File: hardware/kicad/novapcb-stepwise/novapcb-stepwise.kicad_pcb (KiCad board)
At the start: 6 copper layers, 105 x 85 mm, 129 parts, among them J1 USB-C_2.0, J10 CRSF_solder_pad, J11 ESC_solder_pad, J12 ESC_solder_pad, J13 ESC_solder_pad, J14 ESC_solder_pad, J15 ESC_solder_pad, J16 ESC_solder_pad, J17 ESC_solder_pad, J18 ESC_solder_pad, J19 MAUCH2_6P, J2 microSD_DM3AT, J20 CAN_4P, J3 TELEM_6P, J4 MAUCH_6P, J5 GPS_MAG_10P, J9 SWD_10P, Q2 AO3401A, Q3 AO4262E, Q4 AO4262E, Q5 AO3400A, U1 STM32H743VITx, U11 LM74700-Q1, U12 LM74700-Q1, U13 LP5907MFX-3.3, U14 TJA1051TK/3, U15 PESD2CAN, U2 AP2112K-3.3, U3 ICM-42688-P_LGA-14_2.5x3mm_P0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, U4 DPS310, U5 USBLC6-2P6, U6 TPS25940A, U7 LPS22HB, U8 BMI088, U9 LSM6DSV16X, Y1 8MHz

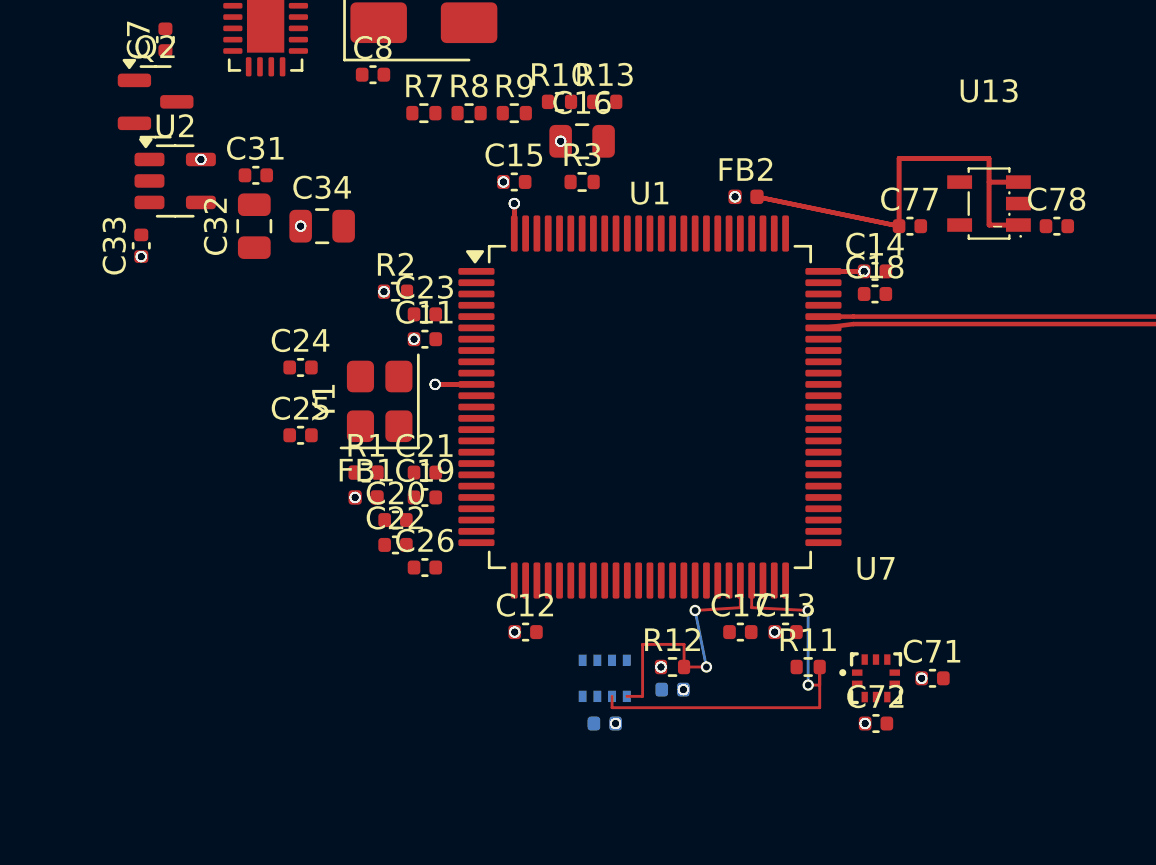
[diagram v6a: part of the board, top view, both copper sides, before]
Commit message: docs+hw: v1.1 6-layer stackup locked, +3V3 moved In4→In3 for B.Cu GND ref
Per master 2026-05-23 directive: articulated per-layer assignment with
explicit SI rationale BEFORE A↔B routing commits a second power plane.

## Final v1.1 stackup (DECISIONS §8)

  L1 F.Cu      — components + high-speed signals (USB diff, I2C2, SPI, DShot)
  L2 In1.Cu    — GND plane (primary)
  L3 In2.Cu    — +5V_BEC plane (NEW for A↔B routing)
  L4 In3.Cu    — +3V3 plane (MOVED from In4 — for B.Cu reference SI)
  L5 In4.Cu    — GND plane (secondary)
  L6 B.Cu      — signals (B.Cu USB sliver, I2C2 sliver, future SDMMC1)

Two GND planes (L2 + L5) sandwich the two power planes. Each signal
layer (L1, L6) has its adjacent reference plane = GND. The two power
planes (L3 +5V, L4 +3V3) are inner-adjacent — they share inter-plane
capacitance as a free HF decoupling cap between rails (acceptable
since +3V3 is derived from +5V via U2 LDO, not DC-isolated).

## Why move +3V3 from In4 to In3

Original PR #72 placed +3V3 on In4. With +3V3 on In4 and B.Cu signals
on L6, B.Cu signals reference +3V3 (not GND). For B.Cu's current 1-2mm
USB diff slivers this is "good enough" but compromises principled SI
for future SDMMC1 (50 MHz) and other high-speed B.Cu routes.

Moving +3V3 to In3 (and putting GND on In4) gives B.Cu a clean GND
reference. Trivial implementation cost: change SetLayer(IN4_CU) to
SetLayer(IN3_CU) in integ_C_B.py.

Thermal impact: zero (gate12 power-injection is layer-independent;
energy balance unaffected).

## SI verification per layer

  F.Cu (L1) → L2 In1 GND adjacent, 0.21mm prepreg — optimal for USB
    87Ω diff pair, I2C2, SPI, DShot.
  B.Cu (L6) → L5 In4 GND adjacent, 0.21mm prepreg — optimal for
    USB B.Cu slivers and future SDMMC1.

Power planes well-decoupled:
  L3 +5V_BEC → L2 GND adjacent above
  L4 +3V3    → L5 GND adjacent below

## Alternatives rejected

| Alternative | Issue |
|---|---|
| 1 GND + 2 power | B.Cu signals see power plane → SI compromise |
| GND-pwr-GND-pwr-GND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
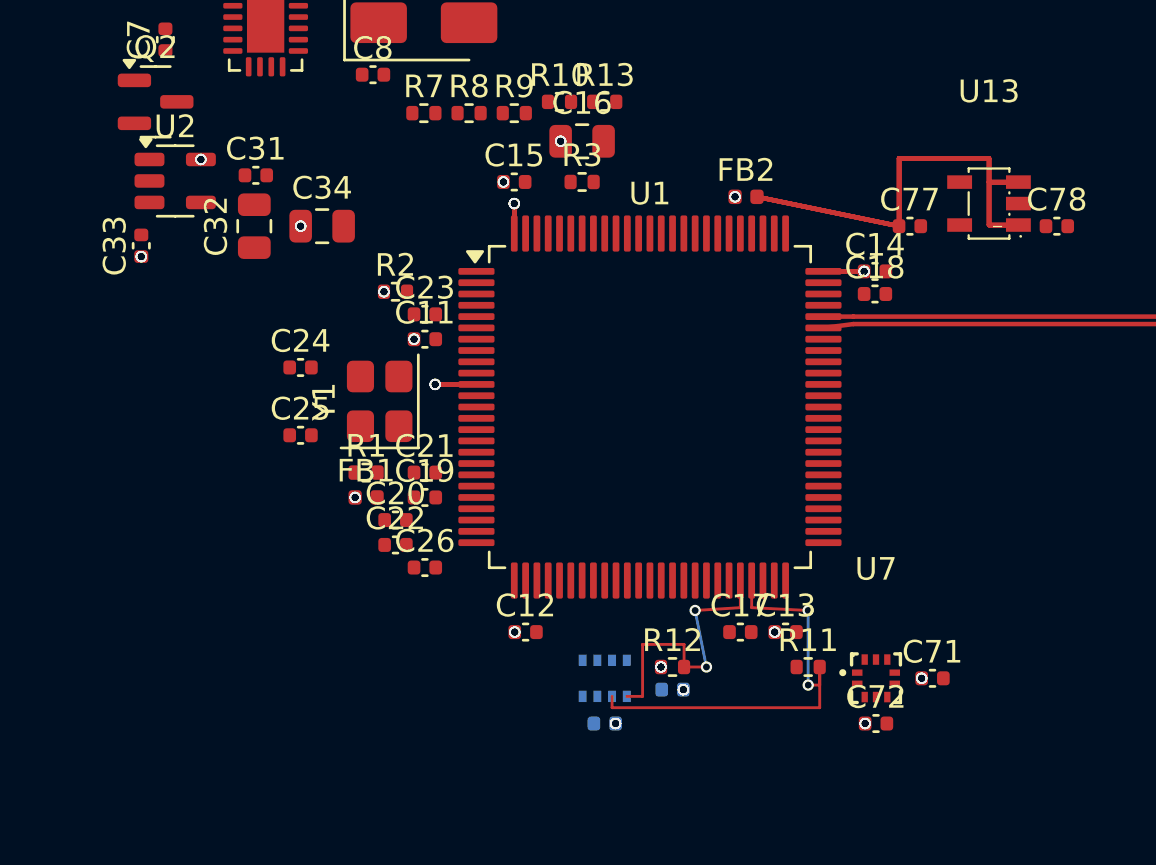
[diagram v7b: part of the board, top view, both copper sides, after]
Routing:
- net +3V3_IMU_PRE: track 37.9 -> 56.8 mm
- net +3V3: track 9.91 -> 14.9 mm, vias 38 -> 57
- added copper zone on In3.Cu, net +3V3
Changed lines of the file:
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@@
+	)
+	(segment
+		(start 52.675 29)
+		(end 54.48 29)
+		(width 0.2)
+		(layer "F.Cu")
+		(net 1)
 	)
 	(segment
@@
 	)
 	(segment
+		(start 39 27.325)
+		(end 39 26)
+		(width 0.2)
+		(layer "F.Cu")
+		(net 1)
+	)
+	(segment
 		(start 37.325 34)
 		(end 35.5 34)
@@
 	)
 	(segment
+		(start 37.325 34)
+		(end 35.5 34)
+		(width 0.2)
+		(layer "F.Cu")
+		(net 1)
+	)
+	(segment
 		(start 52.675 29)
 		(end 54.48 29)
@@
 	)
 	(via
+		(at 29.55 27)
+		(size 0.5)
+		(drill 0.3)
+		(layers "F.Cu" "B.Cu")
+		(net 1)
+	)
+	(via
 		(at 22.5 28.346025)
 		(size 0.5)
@@
 	)
 	(via
+		(at 45.49 46.5)
+		(size 0.5)
+		(drill 0.3)
+		(layers "F.Cu" "B.Cu")
+		(net 1)
+	)
+	(via
 		(at 41.05 23.245)
 		(size 0.5)
@@
 	)
 	(via
+		(at 34.564999 32)
+		(size 0.5)
+		(drill 0.3)
+		(layers "F.Cu" "B.Cu")
+		(net 1)
+	)
+	(via
 		(at 45.49 46.5)
 		(size 0.5)
@@
 	)
 	(via
+		(at 54.475 29)
+		(size 0.5)
+		(drill 0.3)
+		(layers "F.Cu" "B.Cu")
+		(net 1)
+	)
+	(via
 		(at 29.55 27)
 		(size 0.5)
@@
 	)
 	(via
+		(at 39.02 44.955)
+		(size 0.5)
+		(drill 0.3)
+		(layers "F.Cu" "B.Cu")
+		(net 1)
+	)
+	(via
 		(at 38.52 25.045)
 		(size 0.5)
@@
 	)
 	(via
+		(at 39 26)
+		(size 0.5)
+		(drill 0.3)
+		(layers "F.Cu" "B.Cu")
+		(net 1)
+	)
+	(via
 		(at 48.765 25.700961)
 		(size 0.5)
@@
 	)
 	(via
+		(at 48.765 25.700961)
+		(size 0.5)
+		(drill 0.3)
+		(layers "F.Cu" "B.Cu")
+		(net 1)
+	)
+	(via
+		(at 33.235 29.9)
+		(size 0.5)
+		(drill 0.3)
+		(layers "F.Cu" "B.Cu")
+		(net 1)
+	)
+	(via
 		(at 41.05 23.245)
 		(size 0.5)
@@
 	)
 	(via
+		(at 25.1375 24.05)
+		(size 0.5)
+		(drill 0.3)
+		(layers "F.Cu" "B.Cu")
+		(net 1)
+	)
+	(via
 		(at 54.475 29)
 		(size 0.5)
@@
 	)
 	(via
+		(at 31.959999 39)
+		(size 0.5)
+		(drill 0.3)
+		(layers "F.Cu" "B.Cu")
+		(net 1)
+	)
+	(via
 		(at 46.48 47.5)
 		(size 0.5)
@@
 	)
 	(via
+		(at 22.5 28.346025)
+		(size 0.5)
+		(drill 0.3)
+		(layers "F.Cu" "B.Cu")
+		(net 1)
+	)
+	(via
 		(at 57.02 47)
 		(size 0.5)
@@
 	)
 	(via
+		(at 41.05 23.245)
+		(size 0.5)
+		(drill 0.3)
+		(layers "F.Cu" "B.Cu")
+		(net 1)
+	)
+	(via
+		(at 54.52 49)
+		(size 0.5)
+		(drill 0.3)
+		(layers "F.Cu" "B.Cu")
+		(net 1)
+	)
+	(via
 		(at 39 26)
 		(size 0.5)
@@
 	)
 	(via
+		(at 43.48 49)
+		(size 0.5)
+		(drill 0.3)
+		(layers "F.Cu" "B.Cu")
+		(net 1)
+	)
+	(via
+		(at 35.5 34)
+		(size 0.5)
+		(drill 0.3)
+		(layers "F.Cu" "B.Cu")
+		(net 1)
+	)
+	(via
 		(at 25.1375 24.05)
 		(size 0.5)
@@
 	)
 	(via
+		(at 50.52 44.955)
+		(size 0.5)
+		(drill 0.3)
+		(layers "F.Cu" "B.Cu")
+		(net 1)
+	)
+	(via
+		(at 46.48 47.5)
+		(size 0.5)
+		(drill 0.3)
+		(layers "F.Cu" "B.Cu")
+		(net 1)
+	)
+	(via
+		(at 57.02 47)
+		(size 0.5)
+		(drill 0.3)
+		(layers "F.Cu" "B.Cu")
+		(net 1)
+	)
+	(via
 		(at 29.55 27)
 		(size 0.5)
@@
 	(via
 		(at 50.52 44.955)
+		(size 0.5)
+		(drill 0.3)
+		(layers "F.Cu" "B.Cu")
+		(net 1)
+	)
+	(via
+		(at 38.52 25.045)
 		(size 0.5)
 		(drill 0.3)
@@
 	)
 	(segment
+		(start 49.735 25.700961)
+		(end 56.02 27)
+		(width 0.2)
+		(layer "F.Cu")
+		(net 4)
+	)
+	(segment
 		(start 56.02 27)
 		(end 56.02 24)
@@
 	)
 	(segment
+		(start 60 24)
+		(end 60 26.95)
+		(width 0.2)
+		(layer "F.Cu")
+		(net 4)
+	)
+	(segment
 		(start 49.735 25.700961)
 		(end 56.02 27)
@@
 	)
 	(segment
+		(start 56.02 24)
+		(end 60 24)
+		(width 0.2)
+		(layer "F.Cu")
+		(net 4)
+	)
+	(segment
 		(start 61.3 25.05)
 		(end 60 25.05)
@@
 	)
 	(segment
+		(start 61.3 25.05)
+		(end 60 25.05)
+		(width 0.2)
+		(layer "F.Cu")
+		(net 4)
+	)
+	(segment
+		(start 56.02 27)
+		(end 56.02 24)
+		(width 0.2)
+		(layer "F.Cu")
+		(net 4)
+	)
+	(segment
 		(start 56.02 24)
 		(end 60 24)
@@
 	)
 	(segment
+		(start 60 26.95)
+		(end 61.3 26.95)
+		(width 0.2)
+		(layer "F.Cu")
+		(net 4)
+	)
+	(segment
 		(start 49 43.875)
 		(end 47 44)
@@
 	)
 	(zone
+		(net 1)
+		(net_name "+3V3")
+		(layer "In3.Cu")
+		(hatch edge 0.5)
+		(connect_pads
+			(clearance 0.5)
+		)
+		(min_thickness 0.25)
+		(filled_areas_thickness no)
+		(fill
+			(thermal_gap 0.5)
+			(thermal_bridge_width 0.5)
+		)
+		(polygon
+			(pts
+				(xy 15 18) (xy 95 18) (xy 95 52) (xy 15 52)
+			)
+		)
+	)
+	(zone

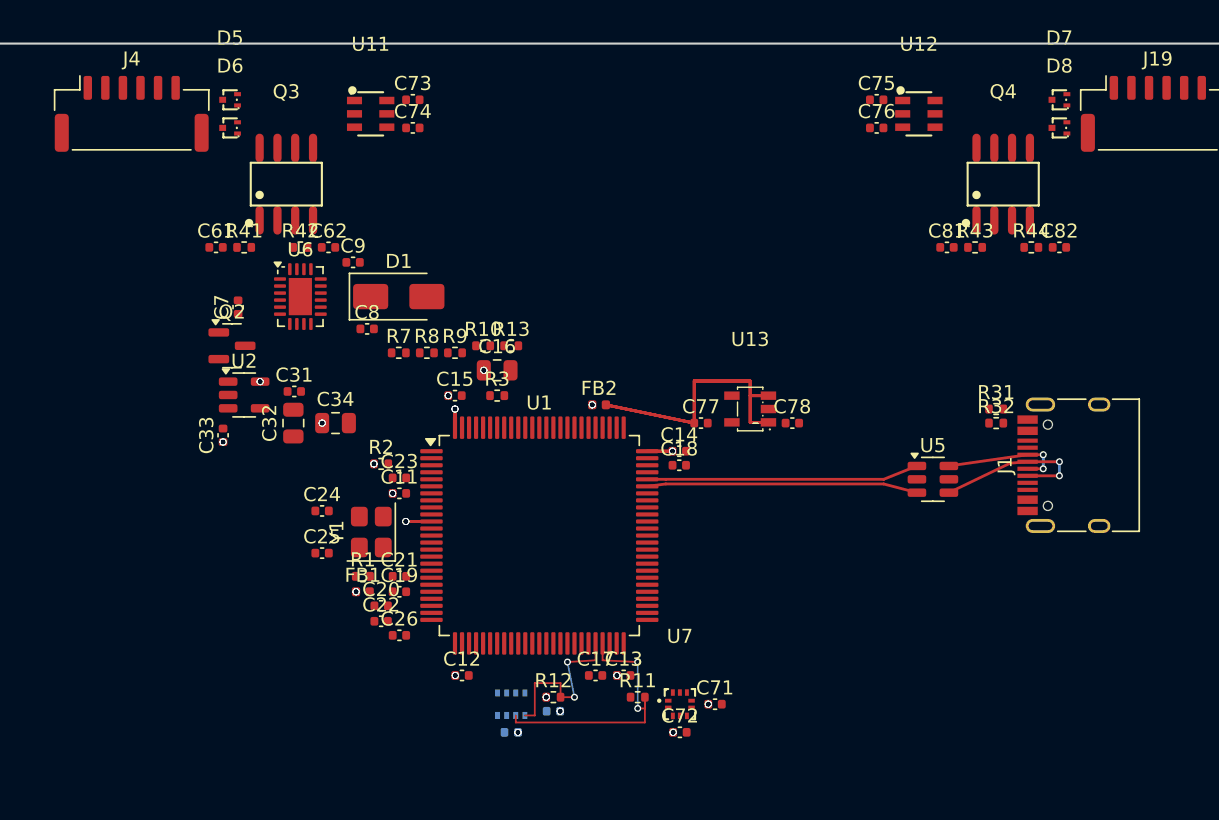
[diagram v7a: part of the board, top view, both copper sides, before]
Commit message: hw: A↔B routing — +5V_BEC plane on In2.Cu + J4/J19 → Q3/Q4 source
Per master 2026-05-23 sign-off after stackup lock (DECISIONS §8).
DRC=0 on this routing scope, 178 unconnected (8 sense + U11/U12 fanout
deferred — see below).

Routes in this PR:
1. **+5V_BEC plane on In2.Cu** — outline X=18..82, Y=6..24. 9 vias at
   Q3.5-8 + Q4.5-8 + Q2.2 drop to the plane. This is the main A↔B
   contract: ≥3A peak carried on full inner-layer plane, low IR drop,
   low loop inductance for OR-FET switching transients.
2. **+5V_BEC_A trunk J4 → Q3 source** — F.Cu trace J4.1+J4.2 → Y=9
   trunk → Q3.3 → Q3.2 → Q3.1 (Q3 source-side bridge).
3. **+5V_BEC_B trunk J19 → Q4 source** — mirror of (2).

DEFERRED (honest framing per master directive — same as C↔B PR #72):

  **U11/U12 SOT-23-6 fanout** — 3 nets per side (ORING_VCAP, GND,
    ORING_GATE on one; +5V_BEC, ORING_A/B_GATE, +5V_BEC_A/B on other)
    at 0.95mm pitch. Attempted F.Cu, B.Cu, and mixed routing — each
    config crosses or shorts adjacent IC pads. Needs:
      (a) U11/U12 re-orientation/relocation for better fanout angle, or
      (b) via-in-pad process for fine-pitch escape, or
      (c) manual route iteration with non-standard via dia
    Without this fanout, OR-FET control is non-functional but plane +
    Q3/Q4 source paths are clean. Functional OR-FET handoff in A↔B-2
    sub-step. Spatially correct now.

  **Sense V/I traces (8 traces total)** — MAUCH_VBAT/CURR_PRE +
    BATT_VOLTAGE/CURRENT_SENS + BATT2 variants. Cross +3V3 stub on
    F.Cu and congest C-zone west side. Defer to a sense sub-step
    using B.Cu with vias near MCU pin or +3V3 stub re-route.

KNOWN UPSTREAM BUG (also noted in PR #72 commit): U6 TPS25922 eFuse
pads have empty net assignments in the SKiDL netlist. The chain
+5V_BEC → U6 → +5V is broken at U6; +5V (U2 LDO input) orphaned.
Filed as SKiDL netlist task — not a PCB routing issue.

Gate 14: GREEN (0 real DRC violations).

Gate 12 v3 thermal: unchanged from A placement step. Heat source
posit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
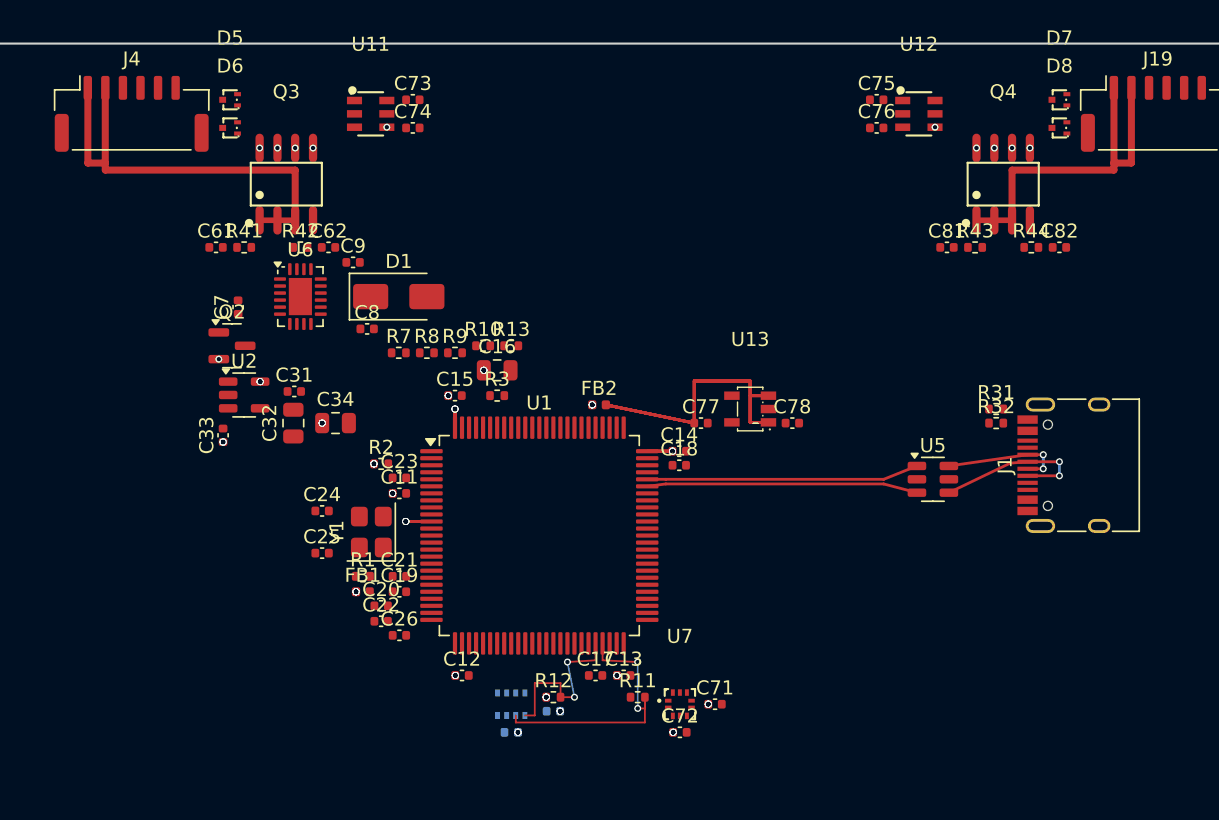
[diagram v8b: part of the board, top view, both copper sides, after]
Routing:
- net +5V_BEC_A: track 0.00 -> 32.0 mm
- net +5V_BEC_B: track 0.00 -> 25.8 mm
- net +3V3_IMU_PRE: track 56.8 -> 75.8 mm
- net +3V3: track 14.9 -> 19.8 mm, vias 57 -> 76
- net +5V_BEC: vias 0 -> 11
- added copper zone on In2.Cu, net +5V_BEC
